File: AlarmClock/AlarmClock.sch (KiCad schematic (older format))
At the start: 40 parts, among them SW1 SW_Push, SW2 SW_Push, SW3 SW_Push, SW4 SW_Push, SW5 SW_Push, U1 7SEGMENT_CA, U1 LM386, U2 7SEGMENT_CA, U3 7SEGMENT_CA, U4 7SEGMENT_CA

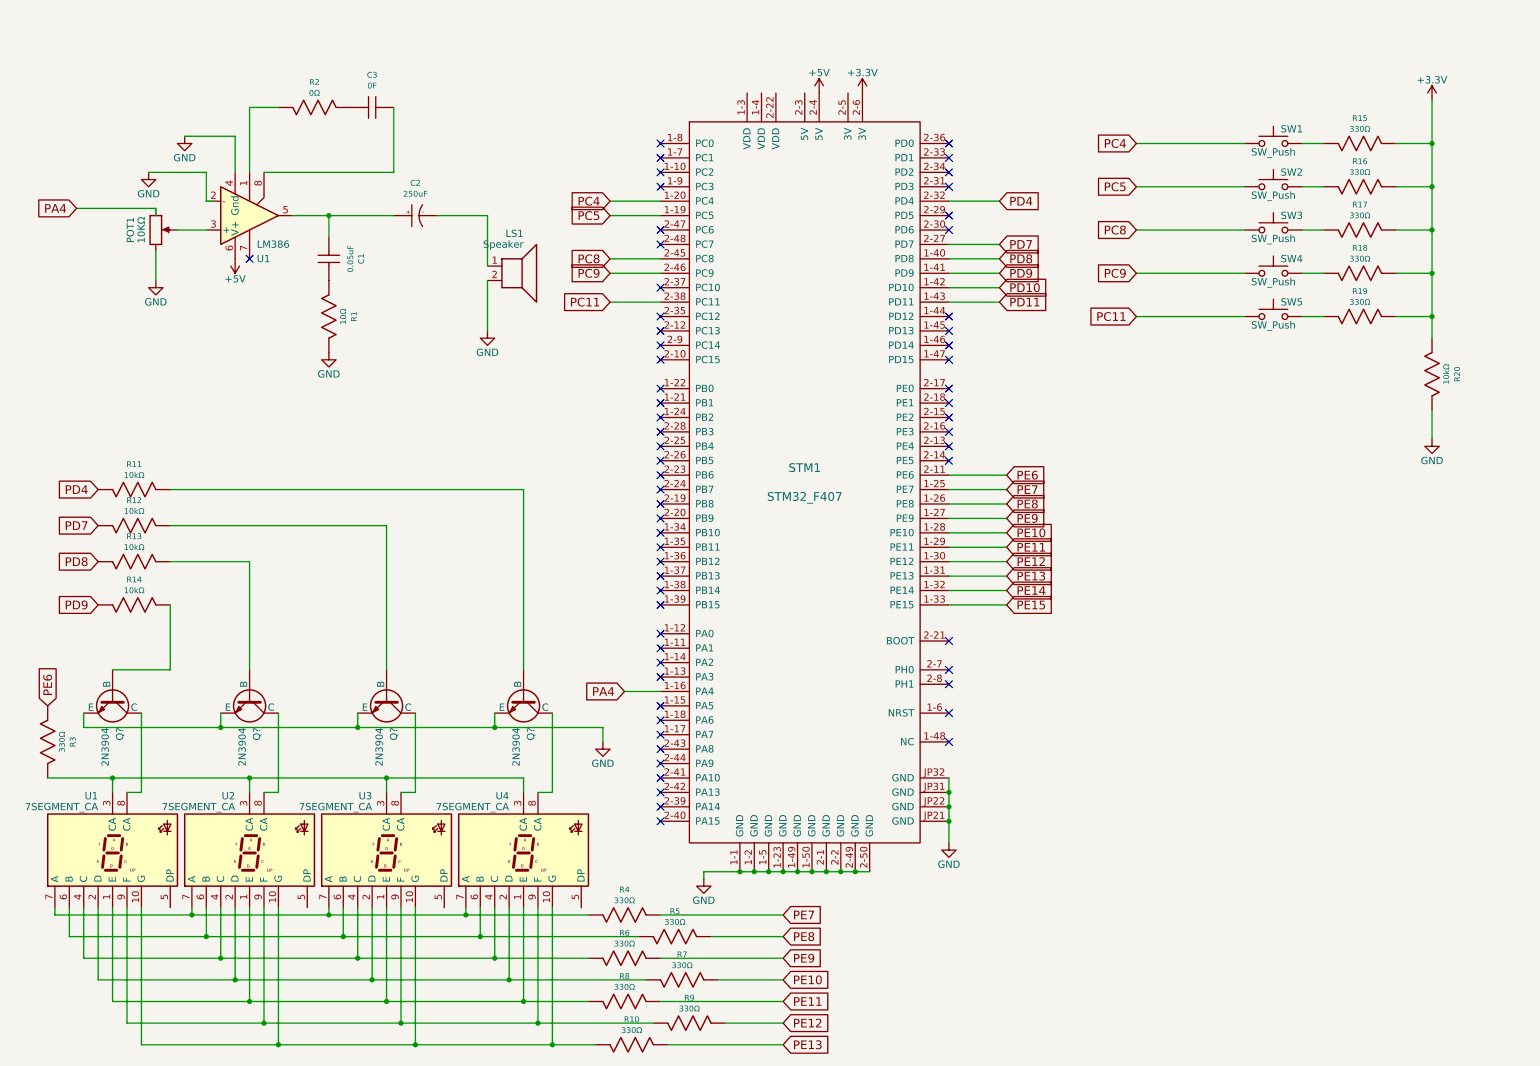
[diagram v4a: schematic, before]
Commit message: finalized for now...
we should add circuit protection and stuff at some point but honestly its probably fine for assignment submission. Also added a cap between supply voltage and ground since as we saw in the lab, that filtered out a lot of the noise in our input signal, kinda guesstimated it but added space for optional capacitor
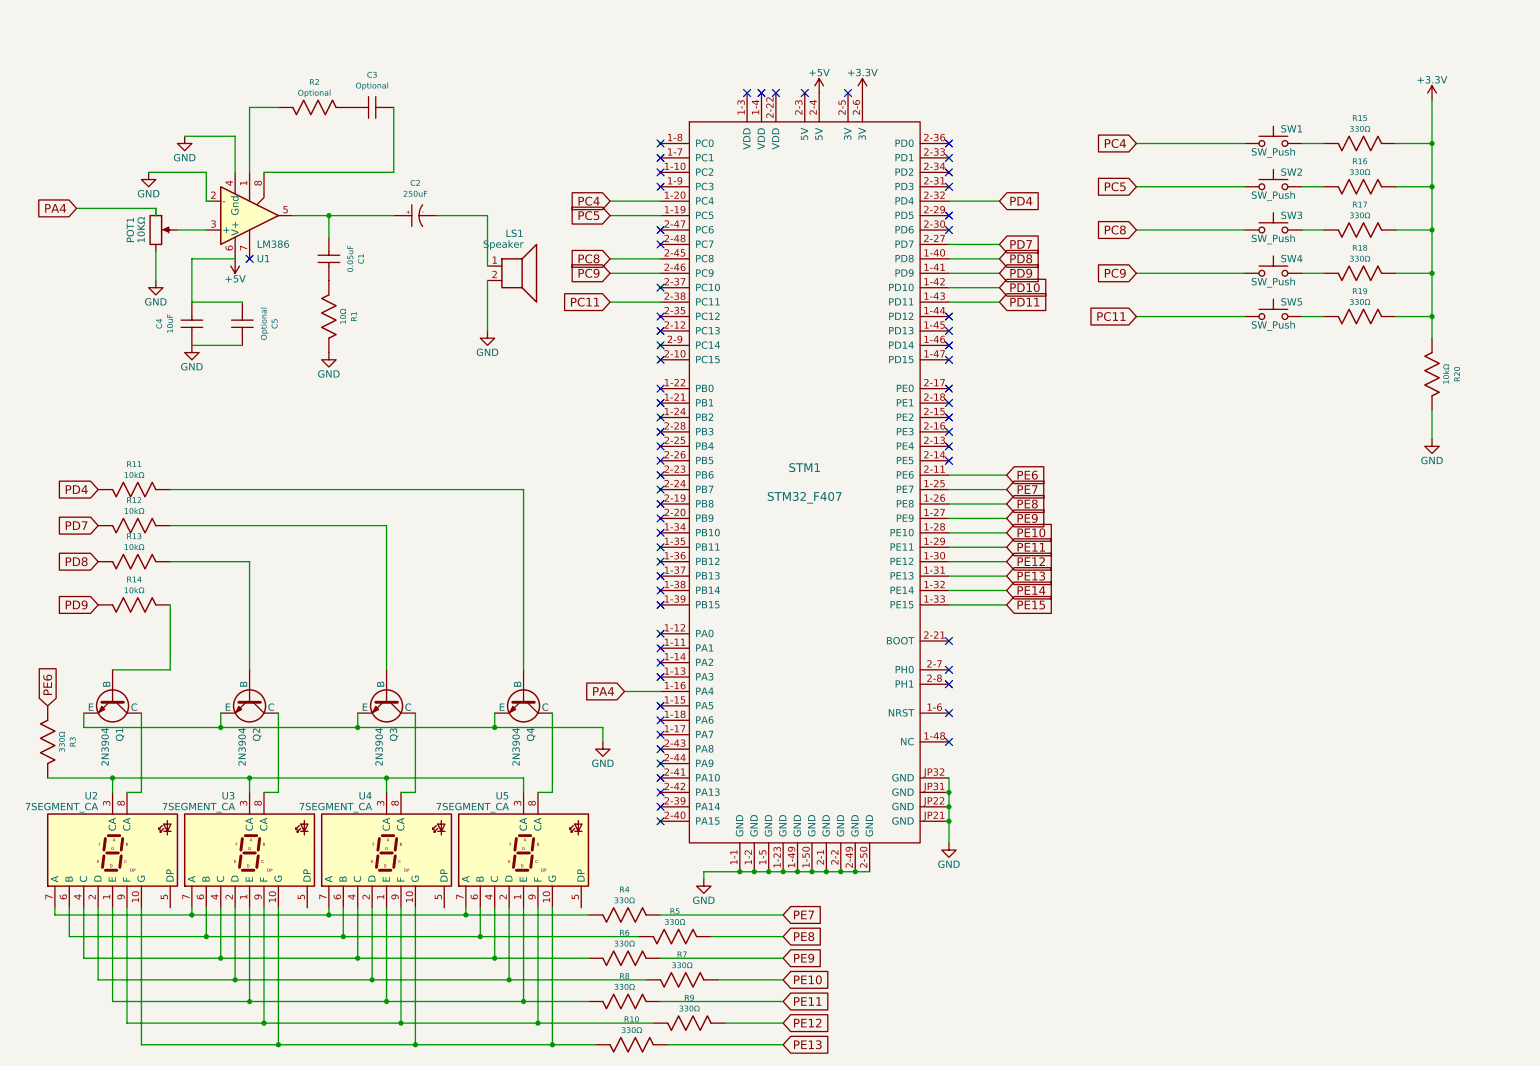
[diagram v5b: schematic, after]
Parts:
- added C4: 10uF, symbol CAP
- added C5: Optional, symbol CAP
- C3: value 0F -> Optional
- R2: value 0Ω -> Optional
- gave numbers to parts that had none: 4
- renumbered U1 to U2, U2 to U3, U3 to U4, U4 to U5
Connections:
- net +5V: now also C4.1, C5.2
- net GND: now also C4.2, C5.1
- no-connect marks 62 -> 67
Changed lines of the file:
@@
 encoding utf-8
 Sheet 1 1
-Title "Alarm Clock PCB"
-Date ""
+Title "ECE 299 Alarm Clock PCB"
+Date "2018-06-22"
 Rev "1.0"
-Comp "Tanner and Ben"
+Comp "Tanner Oleksiuk (V00867082) and Ben Lucas (V00892467)"
 Comment1 ""
 Comment2 ""
@@
 P 2500 1150
 F 0 "R2" H 2500 1325 40  0000 C CNN
-F 1 "0Ω" H 2500 1250 40  0000 C CNN
+F 1 "Optional" H 2500 1250 40  0000 C CNN
 F 2 "" H 2500 1220 30  0000 C CNN
 F 3 "" V 2500 1150 30  0000 C CNN
@@
 P 2900 1150
 F 0 "C3" H 2900 1375 40  0000 C CNN
-F 1 "0F" H 2900 1300 40  0000 C CNN
+F 1 "Optional" H 2900 1300 40  0000 C CNN
 F 2 "" H 2900 1220 30  0000 C CNN
 F 3 "" V 2900 1150 30  0000 C CNN
@@
 $EndComp
 $Comp
-L GND #PWR?
+L GND #PWR01
 U 1 1 5B232F67
 P 1400 2350
-F 0 "#PWR?" H 1400 2100 50  0001 C CNN
+F 0 "#PWR01" H 1400 2100 50  0001 C CNN
 F 1 "GND" H 1400 2200 50  0000 C CNN
 F 2 "" H 1400 2350 50  0001 C CNN
@@
 PA4
 $Comp
-L GND #PWR?
+L GND #PWR02
 U 1 1 5B232FDC
 P 1350 1600
-F 0 "#PWR?" H 1350 1350 50  0001 C CNN
+F 0 "#PWR02" H 1350 1350 50  0001 C CNN
 F 1 "GND" H 1350 1450 50  0000 C CNN
 F 2 "" H 1350 1600 50  0001 C CNN
@@
 $EndComp
 $Comp
-L GND #PWR?
+L GND #PWR03
 U 1 1 5B233010
 P 1600 1350
-F 0 "#PWR?" H 1600 1100 50  0001 C CNN
+F 0 "#PWR03" H 1600 1100 50  0001 C CNN
 F 1 "GND" H 1600 1200 50  0000 C CNN
 F 2 "" H 1600 1350 50  0001 C CNN
@@
 NoConn ~ 2050 2200
 $Comp
-L GND #PWR?
+L GND #PWR04
 U 1 1 5B232F3C
 P 2600 2850
-F 0 "#PWR?" H 2600 2600 50  0001 C CNN
+F 0 "#PWR04" H 2600 2600 50  0001 C CNN
 F 1 "GND" H 2600 2700 50  0000 C CNN
 F 2 "" H 2600 2850 50  0001 C CNN
@@
 $EndComp
 $Comp
-L GND #PWR?
+L GND #PWR05
 U 1 1 5B23335D
 P 3700 2700
-F 0 "#PWR?" H 3700 2450 50  0001 C CNN
+F 0 "#PWR05" H 3700 2450 50  0001 C CNN
 F 1 "GND" H 3700 2550 50  0000 C CNN
 F 2 "" H 3700 2700 50  0001 C CNN
@@
 PD7
 $Comp
-L GND #PWR?
+L GND #PWR06
 U 1 1 5B28351C
 P 5200 6500
-F 0 "#PWR?" H 5200 6250 50  0001 C CNN
+F 0 "#PWR06" H 5200 6250 50  0001 C CNN
 F 1 "GND" H 5200 6350 50  0000 C CNN
 F 2 "" H 5200 6500 50  0001 C CNN
@@
 $EndComp
 $Comp
-L GND #PWR?
+L GND #PWR07
 U 1 1 5B283542
 P 6900 6250
-F 0 "#PWR?" H 6900 6000 50  0001 C CNN
+F 0 "#PWR07" H 6900 6000 50  0001 C CNN
 F 1 "GND" H 6900 6100 50  0000 C CNN
 F 2 "" H 6900 6250 50  0001 C CNN
@@
 NoConn ~ 4900 1400
 $Comp
-L 7SEGMENT_CA U1
+L 7SEGMENT_CA U2
 U 1 1 5B2B2844
 P 1100 6300
-F 0 "U1" H 1000 6675 50  0000 R CNN
+F 0 "U2" H 1000 6675 50  0000 R CNN
 F 1 "7SEGMENT_CA" H 1000 6600 50  0000 R CNN
 F 2 "" H 1550 6000 50  0001 L CNN
@@
 $EndComp
 $Comp
-L 7SEGMENT_CA U2
+L 7SEGMENT_CA U3
 U 1 1 5B2B289D
 P 2050 6300
-F 0 "U2" H 1950 6675 50  0000 R CNN
+F 0 "U3" H 1950 6675 50  0000 R CNN
 F 1 "7SEGMENT_CA" H 1950 6600 50  0000 R CNN
 F 2 "" H 2500 6000 50  0001 L CNN
@@
 $EndComp
 $Comp
-L 7SEGMENT_CA U3
+L 7SEGMENT_CA U4
 U 1 1 5B2B28F6
 P 3000 6300
-F 0 "U3" H 2900 6675 50  0000 R CNN
+F 0 "U4" H 2900 6675 50  0000 R CNN
 F 1 "7SEGMENT_CA" H 2900 6600 50  0000 R CNN
 F 2 "" H 3450 6000 50  0001 L CNN
@@
 $EndComp
 $Comp
-L 7SEGMENT_CA U4
+L 7SEGMENT_CA U5
 U 1 1 5B2B2953
 P 3950 6300
-F 0 "U4" H 3850 6675 50  0000 R CNN
+F 0 "U5" H 3850 6675 50  0000 R CNN
 F 1 "7SEGMENT_CA" H 3850 6600 50  0000 R CNN
 F 2 "" H 4400 6000 50  0001 L CNN
@@
 PE6
 $Comp
-L 2N3904 Q?
+L 2N3904 Q1
 U 1 1 5B2B526F
 P 1100 5300
-F 0 "Q?" H 1250 5350 50  0000 L CNN
+F 0 "Q1" H 1250 5350 50  0000 L CNN
 F 1 "2N3904" H 1250 5250 50  0000 L CNN
 F 2 "" H 1250 5225 50  0000 L CIN
@@
 $EndComp
 $Comp
-L 2N3904 Q?
+L 2N3904 Q2
 U 1 1 5B2B5484
 P 2050 5300
-F 0 "Q?" H 2200 5350 50  0000 L CNN
+F 0 "Q2" H 2200 5350 50  0000 L CNN
 F 1 "2N3904" H 2200 5250 50  0000 L CNN
 F 2 "" H 2200 5225 50  0000 L CIN
@@
 $EndComp
 $Comp
-L 2N3904 Q?
+L 2N3904 Q3
 U 1 1 5B2B550F
 P 3000 5300
-F 0 "Q?" H 3150 5350 50  0000 L CNN
+F 0 "Q3" H 3150 5350 50  0000 L CNN
 F 1 "2N3904" H 3150 5250 50  0000 L CNN
 F 2 "" H 3150 5225 50  0000 L CIN
@@
 $EndComp
 $Comp
-L 2N3904 Q?
+L 2N3904 Q4
 U 1 1 5B2B557E
 P 3950 5300
-F 0 "Q?" H 4100 5350 50  0000 L CNN
+F 0 "Q4" H 4100 5350 50  0000 L CNN
 F 1 "2N3904" H 4100 5250 50  0000 L CNN
 F 2 "" H 4100 5225 50  0000 L CIN
@@
 $EndComp
 $Comp
-L GND #PWR?
+L GND #PWR08
 U 1 1 5B2B658D
 P 4500 5550
-F 0 "#PWR?" H 4500 5300 50  0001 C CNN
+F 0 "#PWR08" H 4500 5300 50  0001 C CNN
 F 1 "GND" H 4500 5400 50  0000 C CNN
 F 2 "" H 4500 5550 50  0001 C CNN
@@
 $EndComp
 $Comp
-L GND #PWR?
+L GND #PWR09
 U 1 1 5B2BE1EF
 P 10250 3450
-F 0 "#PWR?" H 10250 3200 50  0001 C CNN
+F 0 "#PWR09" H 10250 3200 50  0001 C CNN
 F 1 "GND" H 10250 3300 50  0000 C CNN
 F 2 "" H 10250 3450 50  0001 C CNN
@@
 $EndComp
 $Comp
-L +3.3V #PWR?
+L +3.3V #PWR010
 U 1 1 5B2BF6D3
 P 10250 1100
-F 0 "#PWR?" H 10250 950 50  0001 C CNN
+F 0 "#PWR010" H 10250 950 50  0001 C CNN
 F 1 "+3.3V" H 10250 1240 50  0000 C CNN
 F 2 "" H 10250 1100 50  0001 C CNN
@@
 $EndComp
 $Comp
-L +3.3V #PWR?
+L +3.3V #PWR011
 U 1 1 5B2BF7FF
 P 6300 1050
-F 0 "#PWR?" H 6300 900 50  0001 C CNN
+F 0 "#PWR011" H 6300 900 50  0001 C CNN
 F 1 "+3.3V" H 6300 1190 50  0000 C CNN
 F 2 "" H 6300 1050 50  0001 C CNN
@@
 $EndComp
 $Comp
-L +5V #PWR?
+L +5V #PWR012
 U 1 1 5B2BF88B
 P 6000 1050
-F 0 "#PWR?" H 6000 900 50  0001 C CNN
+F 0 "#PWR012" H 6000 900 50  0001 C CNN
 F 1 "+5V" H 6000 1190 50  0000 C CNN
 F 2 "" H 6000 1050 50  0001 C CNN
@@
 $EndComp
 $Comp
-L +5V #PWR?
+L +5V #PWR013
 U 1 1 5B2BF9B7
 P 1950 2200
-F 0 "#PWR?" H 1950 2050 50  0001 C CNN
+F 0 "#PWR013" H 1950 2050 50  0001 C CNN
 F 1 "+5V" H 1950 2340 50  0000 C CNN
 F 2 "" H 1950 2200 50  0001 C CNN
@@
 Wire Wire Line
 	3350 1900 3700 1900
+NoConn ~ 5500 1050
+NoConn ~ 5600 1050
+NoConn ~ 5700 1050
+NoConn ~ 5900 1050
+NoConn ~ 6200 1050
+Wire Wire Line
+	1950 2200 1650 2200
+Wire Wire Line
+	1650 2200 1650 2500
+$Comp
+L CAP C4
+U 1 1 5B2C8A03
+P 1650 2650
+F 0 "C4" H 1650 2875 40  0000 C CNN
+F 1 "10uF" H 1650 2800 40  0000 C CNN
+F 2 "" H 1650 2720 30  0000 C CNN
+F 3 "" V 1650 2650 30  0000 C CNN
+	1    1650 2650
+	0    -1   -1   0
+$EndComp
+$Comp
+L GND #PWR?
+U 1 1 5B2C8D6B
+P 1650 2800
+F 0 "#PWR?" H 1650 2550 50  0001 C CNN
+F 1 "GND" H 1650 2650 50  0000 C CNN
+F 2 "" H 1650 2800 50  0001 C CNN
+F 3 "" H 1650 2800 50  0001 C CNN
+	1    1650 2800
+	1    0    0    -1
+$EndComp
+Wire Wire Line
+	1650 2500 2000 2500
+$Comp
+L CAP C5
+U 1 1 5B2C9594
+P 2000 2650
+F 0 "C5" H 2000 2875 40  0000 C CNN
+F 1 "Optional" H 2000 2800 40  0000 C CNN
+F 2 "" H 2000 2720 30  0000 C CNN
+F 3 "" V 2000 2650 30  0000 C CNN
+	1    2000 2650
+	0    1    1    0
+$EndComp
+Wire Wire Line
+	2000 2800 1650 2800
 $EndSCHEMATC

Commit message: fixed op amp circuit and 7-seg
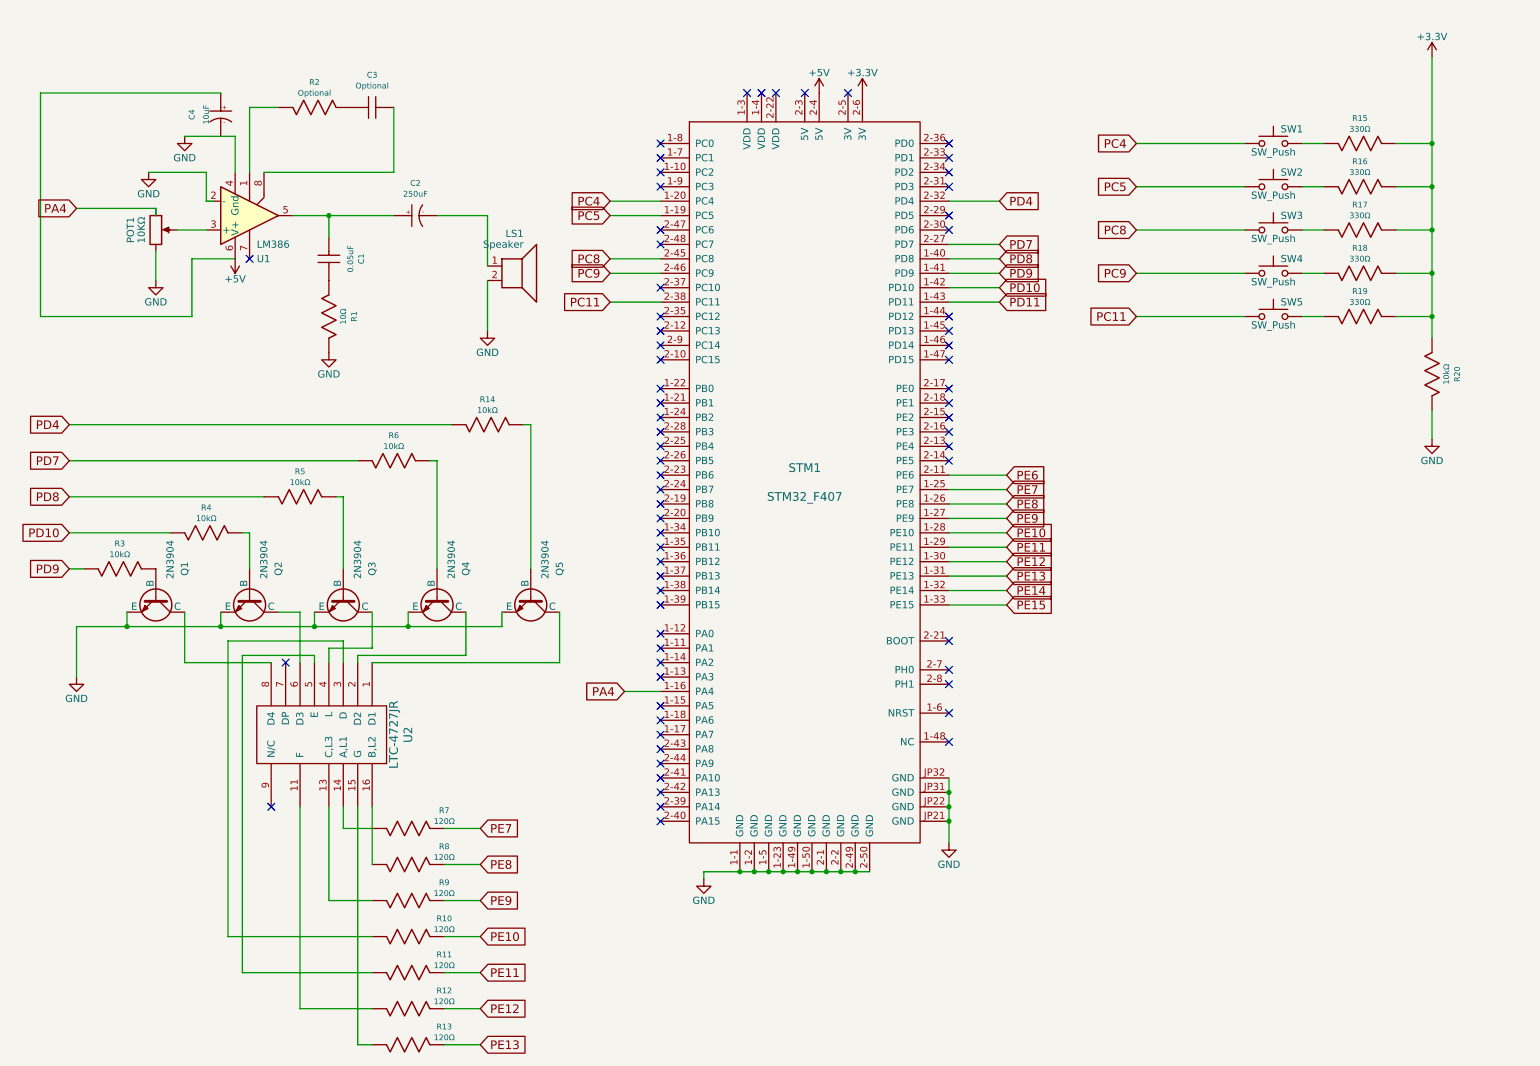
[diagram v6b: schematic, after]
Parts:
- removed C4: 10uF, symbol CAP
- removed C5: Optional, symbol CAP
- removed U2, U3, U4, U5: 7SEGMENT_CA, symbol 7SEGMENT_CA
- added C4: 10uF, symbol CAP_POL
- added Q5: 2N3904, symbol 2N3904
- added U2: LTC-4727JR, symbol LTC-4727JR
- R10, R7, R8, R9: value 330Ω -> 120Ω
- R11, R12, R13: value 10kΩ -> 120Ω
- R3, R4, R5, R6: value 330Ω -> 10kΩ
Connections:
- net +5V: now also C4.1 (+)
- net GND: now also Q5.1 (E)
- net PD10: now also R4.2
- net PD4: now also R14.2; no longer R11.2
- net PD7: now also R6.2; no longer R12.2
- net PD8: now also R5.2; no longer R13.2
- net PD9: now also R3.2; no longer R14.2
- net PE10: now also R10.1; no longer R7.1
- net PE11: now also R11.1; no longer R8.1
- net PE12: now also R12.1; no longer R9.1
- net PE13: now also R13.1; no longer R10.1
- net PE6: no longer R3.2
- net PE7: now also R7.1; no longer R4.1
- net PE8: now also R8.1; no longer R5.1
- net PE9: now also R9.1; no longer R6.1
- net at R8.2: now also U2.16 (B,L2)
- net at R10.2: now also U2.3 (D)
- net at R7.2: now also U2.14 (A,L1)
- net at R3.1: now also Q1.2 (B)
- net at Q1.3 (C): now also U2.8 (D4)
- net at R9.2: now also U2.13 (C,L3)
- net at Q2.3 (C): now also U2.6 (D3)
- net at Q3.3 (C): now also U2.4 (L)
- net at Q4.3 (C): now also U2.2 (D2)
- net at Q4.2 (B): now also R6.1; no longer R11.1
- net at Q3.2 (B): now also R5.1; no longer R12.1
- net at Q2.2 (B): now also R4.1; no longer R13.1
- net at R14.1: now also Q5.2 (B); no longer Q1.2 (B)
- new net: Q5.3 (C), U2.1 (D1)
- new net: R12.2, U2.11 (F)
- new net: R13.2, U2.15 (G)
- new net: R11.2, U2.5 (E)
- no-connect marks 67 -> 69

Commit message: Modified schematic to include low pass filter and removed PB circuit
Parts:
- removed R16, R17, R18, R19: 330Ω, symbol RES
- removed R20: 10kΩ, symbol RES
- removed SW1, SW2, SW3, SW4, SW5: SW_Push, symbol SW_Push
- added C5: 1nF, symbol CAP
- added U3: LM358, symbol LM358
- C3: value Optional -> 1nF
- Q1, Q2, Q3, Q4, Q5: symbol 2N3904 -> 2N3904-RESCUE-AlarmClock
- R15: value 330Ω -> 20kΩ
- R2: value Optional -> 20kΩ
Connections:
- net +3V3: now also U3.8 (V+); no longer R15.1
- net GND: now also C3.2, U3.4 (V-)
- net PA4: now also R2.2; no longer POT1.1
- net at U1.1: no longer R2.2
- net at U1.8: no longer C3.1
- net at R2.1: now also R15.2, C5.2; no longer C3.2
- new net: C3.1, R15.1, U3.3 (+)
- new net Vf: POT1.1, U3.1, U3.2 (-)

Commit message: final schem
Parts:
- added R16: 200Ω, symbol RES
- R14, R3, R4, R5, R6: value 10kΩ -> 1kΩ
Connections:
- net at C1.1, C2.1 (+): now also R16.2; no longer U1.5
- new net: R16.1, U1.5
- no-connect marks 69 -> 71
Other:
- moved on the sheet: C1, R1
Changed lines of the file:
@@
 L RES R1
 U 1 1 5B232694
-P 2600 2600
-F 0 "R1" H 2600 2775 40  0000 C CNN
-F 1 "10Ω" H 2600 2700 40  0000 C CNN
-F 2 "" H 2600 2670 30  0000 C CNN
-F 3 "" V 2600 2600 30  0000 C CNN
-	1    2600 2600
+P 2900 2600
+F 0 "R1" H 2900 2775 40  0000 C CNN
+F 1 "10Ω" H 2900 2700 40  0000 C CNN
+F 2 "" H 2900 2670 30  0000 C CNN
+F 3 "" V 2900 2600 30  0000 C CNN
+	1    2900 2600
 	0    1    1    0
 $EndComp
@@
 L CAP C1
 U 1 1 5B23285D
-P 2600 2200
-F 0 "C1" H 2600 2425 40  0000 C CNN
-F 1 "0.05uF" H 2600 2350 40  0000 C CNN
-F 2 "" H 2600 2270 30  0000 C CNN
-F 3 "" V 2600 2200 30  0000 C CNN
-	1    2600 2200
+P 2900 2200
+F 0 "C1" H 2900 2425 40  0000 C CNN
+F 1 "0.05uF" H 2900 2350 40  0000 C CNN
+F 2 "" H 2900 2270 30  0000 C CNN
+F 3 "" V 2900 2200 30  0000 C CNN
+	1    2900 2200
 	0    1    -1   0
 $EndComp
@@
 L GND #PWR6
 U 1 1 5B232F3C
-P 2600 2850
-F 0 "#PWR6" H 2600 2600 50  0001 C CNN
-F 1 "GND" H 2600 2700 50  0000 C CNN
-F 2 "" H 2600 2850 50  0001 C CNN
-F 3 "" H 2600 2850 50  0001 C CNN
-	1    2600 2850
+P 2900 2850
+F 0 "#PWR6" H 2900 2600 50  0001 C CNN
+F 1 "GND" H 2900 2700 50  0000 C CNN
+F 2 "" H 2900 2850 50  0001 C CNN
+F 3 "" H 2900 2850 50  0001 C CNN
+	1    2900 2850
 	1    0    0    -1
 $EndComp
@@
 	1950 1350 1600 1350
 Wire Wire Line
-	2350 1900 3050 1900
-Wire Wire Line
-	2600 1900 2600 2050
-Connection ~ 2600 1900
+	2900 1900 2900 2050
 Wire Wire Line
 	3700 1900 3700 2250
@@
 P 3050 3600
 F 0 "R6" H 3050 3775 40  0000 C CNN
-F 1 "10kΩ" H 3050 3700 40  0000 C CNN
+F 1 "1kΩ" H 3050 3700 40  0000 C CNN
 F 2 "" H 3050 3670 30  0000 C CNN
 F 3 "" V 3050 3600 30  0000 C CNN
@@
 P 2400 3850
 F 0 "R5" H 2400 4025 40  0000 C CNN
-F 1 "10kΩ" H 2400 3950 40  0000 C CNN
+F 1 "1kΩ" H 2400 3950 40  0000 C CNN
 F 2 "" H 2400 3920 30  0000 C CNN
 F 3 "" V 2400 3850 30  0000 C CNN
@@
 P 1750 4100
 F 0 "R4" H 1750 4275 40  0000 C CNN
-F 1 "10kΩ" H 1750 4200 40  0000 C CNN
+F 1 "1kΩ" H 1750 4200 40  0000 C CNN
 F 2 "" H 1750 4170 30  0000 C CNN
 F 3 "" V 1750 4100 30  0000 C CNN
@@
 P 3700 3350
 F 0 "R14" H 3700 3525 40  0000 C CNN
-F 1 "10kΩ" H 3700 3450 40  0000 C CNN
+F 1 "1kΩ" H 3700 3450 40  0000 C CNN
 F 2 "" H 3700 3420 30  0000 C CNN
 F 3 "" V 3700 3350 30  0000 C CNN
@@
 P 1150 4350
 F 0 "R3" H 1150 4525 40  0000 C CNN
-F 1 "10kΩ" H 1150 4450 40  0000 C CNN
+F 1 "1kΩ" H 1150 4450 40  0000 C CNN
 F 2 "" H 1150 4420 30  0000 C CNN
 F 3 "" V 1150 4350 30  0000 C CNN
@@
 Text GLabel 10650 1700 2    60   Input ~ 0
 Vf
+NoConn ~ 2050 1600
+NoConn ~ 2150 1600
+Connection ~ 2900 1900
+$Comp
+L RES R16
+U 1 1 5B36FE4D
+P 2600 1900
+F 0 "R16" H 2600 2075 40  0000 C CNN
+F 1 "200Ω" H 2600 2000 40  0000 C CNN
+F 2 "" H 2600 1970 30  0000 C CNN
+F 3 "" V 2600 1900 30  0000 C CNN
+	1    2600 1900
+	-1   0    0    1
+$EndComp
+Wire Wire Line
+	2850 1900 3050 1900
 $EndSCHEMATC
